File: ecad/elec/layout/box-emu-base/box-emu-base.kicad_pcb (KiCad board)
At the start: 2 copper layers, 72.5 x 63.9 mm, 66 parts

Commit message: feat(ecad): Update ecad / atopile and improve workflow
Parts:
- removed DS1: , lib:SOD-323_L1.8-W1.3-LS2.5-RD
- removed J1: , lib:CONN-SMD_4P-P1.00_SM04B-SRSS-TB-LF-SN
- removed R27: 62.5mW Thick Film Resistors 50V ±100ppm/℃ ±1% 249Ω 0402 Chi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, lib:R0402
- removed U10: , Connector_PinHeader_1.00mm:PinHeader_1x02_P1.00mm_Vertical
- removed U11: , lib:GAMEBOY_COLOR_DPAD_MEMBRANE
- removed U12, U13, U14, U15: , lib:GBC_DPAD_BUTTON
- removed U16, U19: , lib:GAMEBOY_COLOR_A_B_BUTTON_MEMBRANE
- removed U17, U18, U20, U21: , lib:GBC_A_B_BUTTON
- removed U22: , lib:GAMEBOY_COLOR_START_SELECT_MEMBRANE
- removed U23, U24: , lib:GBC_START_SELECT_BUTTON
- removed U25, U26: , lib:SW-SMD_TS24CA
- removed U7: , lib:DFN-8_L2.0-W2.0-P0.50-BL-EP
- removed U8: , lib:SIM-SMD_C9900007362
- removed U9: , lib:VSSOP-10_L3.0-W3.0-P0.50-LS4.9-BL
- added C10: 22µF ±20%, Samsung_Electro_Mechanics_CL21A226MAQNNNE:C0805, F.Cu at (300.0, -290.0)
- added C11: 22µF ±20%, Samsung_Electro_Mechanics_CL21A226MAQNNNE:C0805, F.Cu at (300.0, -300.0)
- added C12: 100nF ±10%, Samsung_Electro_Mechanics_CL05B104KO5NNNC:C0402, F.Cu at (300.0, -330.0)
- added C13: 100nF ±10%, Samsung_Electro_Mechanics_CL05B104KO5NNNC:C0402, F.Cu at (300.0, -340.0)
- added CN1: , JST_Sales_America_S2B_PH_SM4_TB_LF__SN:CONN-SMD_P2.00_S2B-PH-SM4-TB-LF-SN, B.Cu at (-11.2, 58.3)
- added CN2: , JST_Sales_America_SM04B_SRSS_TB_LF__SN:CONN-SMD_4P-P1.00_SM04B-SRSS-TB-LF-SN, F.Cu at (30.0, 0.00)
- added D1: , Guangdong_Hottech_1N5819WS:SOD-323_L1.8-W1.3-LS2.5-RD, F.Cu at (-14.1, 51.3)
- added H1: , Ckmtw_B_2100S02P_A110:HDR-TH_2P-P2.54-V-M-1, F.Cu at (1.15, 2.39)
- added MECH1: , GBC_A_B_MEMBRANE:GAMEBOY_COLOR_A_B_BUTTON_MEMBRANE, F.Cu at (21.2, 29.4)
- added MECH2: , GBC_A_B_MEMBRANE:GAMEBOY_COLOR_A_B_BUTTON_MEMBRANE, F.Cu at (15.9, 14.2)
- added MECH3: , GBC_DPAD_MEMBRANE:GAMEBOY_COLOR_DPAD_MEMBRANE, F.Cu at (-22.9, 21.8)
- added MECH4: , BOX_EMU_BASE_OUTLINE:BOX_EMU_BASE, F.Cu at (0.00, 0.00)
- added MECH5: , GBC_START_SELECT_MEMBRANE:GAMEBOY_COLOR_START_SELECT_MEMBRANE, F.Cu at (-1.52, 44.0)
- added SW1: , GBC_A_B_BUTTON:GBC_A_B_BUTTON, F.Cu at (28.1, 27.0)
- added SW10: , GBC_START_SELECT_BUTTON:GBC_START_SELECT_BUTTON, F.Cu at (4.70, 44.0)
- added SW11: , SHOU_HAN_TS24CA:SW-SMD_2P-TS24CA, F.Cu at (-21.8, 62.7)
- added SW12: , SHOU_HAN_TS24CA:SW-SMD_2P-TS24CA, F.Cu at (-15.8, 63.7)
- added SW2: , GBC_A_B_BUTTON:GBC_A_B_BUTTON, F.Cu at (14.2, 32.0)
- added SW3: , GBC_A_B_BUTTON:GBC_A_B_BUTTON, F.Cu at (23.0, 11.7)
- added SW4: , GBC_A_B_BUTTON:GBC_A_B_BUTTON, F.Cu at (9.01, 16.6)
- added SW5: , GBC_DPAD_BUTTON:GBC_DPAD_BUTTON, F.Cu at (-22.9, 29.8)
- added SW6: , GBC_DPAD_BUTTON:GBC_DPAD_BUTTON, F.Cu at (-30.9, 21.9)
- added SW7: , GBC_DPAD_BUTTON:GBC_DPAD_BUTTON, F.Cu at (-14.9, 21.9)
- added SW8: , GBC_DPAD_BUTTON:GBC_DPAD_BUTTON, F.Cu at (-22.9, 13.9)
- added SW9: , GBC_START_SELECT_BUTTON:GBC_START_SELECT_BUTTON, F.Cu at (-6.86, 44.0)
- added USB1: , Yuandi_TYPE_611_T3_W:USB-C-SMD_TYPE-611-T3-W, F.Cu at (-1.14, 63.9)
- C1: value 16V 100nF X7R ±10% 0402 Multilayer Ceramic Capacitors MLCC - SMD/SMT ROHS -> 100nF ±10%; footprint lib:C0402 -> Samsung_Electro_Mechanics_CL05B104KO5NNNC:C0402
- C2: value 25V 10uF X5R ±10% 0805 Multilayer Ceramic Capacitors MLCC - SMD/SMT ROHS -> 1µF ±10%; footprint lib:C0805 -> Samsung_Electro_Mechanics_CL05A105KA5NQNC:C0402
- C3, C4, C5: value 25V 10uF X5R ±10% 0805 Multilayer Ceramic Capacitors MLCC - SMD/SMT ROHS -> 100nF ±10%; footprint lib:C0805 -> Samsung_Electro_Mechanics_CL05B104KO5NNNC:C0402
- C6: value 16V 100nF X7R ±10% 0402 Multilayer Ceramic Capacitors MLCC - SMD/SMT ROHS -> 4.7µF ±10%; footprint lib:C0402 -> Samsung_Electro_Mechanics_CL05A475KP5NRNC:C0402
- C7: value 10V 4.7uF X5R ±20% 0402 Multilayer Ceramic Capacitors MLCC - SMD/SMT ROHS -> 4.7µF ±10%; footprint lib:C0402 -> Samsung_Electro_Mechanics_CL05A475KP5NRNC:C0402
- C8: value 10V 4.7uF X5R ±20% 0402 Multilayer Ceramic Capacitors MLCC - SMD/SMT ROHS -> 10µF ±10%; footprint lib:C0402 -> Samsung_Electro_Mechanics_CL21A106KAYNNNE:C0805
- C9: value 16V 100nF X7R ±10% 0402 Multilayer Ceramic Capacitors MLCC - SMD/SMT ROHS -> 10µF ±10%; footprint lib:C0402 -> Samsung_Electro_Mechanics_CL21A106KAYNNNE:C0805
- L1: footprint lib:IND-SMD_L2.5-W2.0_WPN252012H -> Sunlord_WPN252012H1R5MT:IND-SMD_L2.5-W2.0_WPN252012H
- LED1: footprint lib:LED0805-R-RD -> Yongyu_Photoelectric_SZYY0805R:LED0805-R-RD
- R1, R2: value 62.5mW Thick Film Resistors 50V ±100ppm/℃ ±1% 4.7kΩ 0402 Chip Resistor - Surface Mount ROHS -> 1MΩ ±1%; footprint lib:R0402 -> UNI_ROYAL_0402WGF1004TCE:R0402
- R10: value 62.5mW Thick Film Resistors 50V ±100ppm/℃ ±1% 2kΩ 0402 Chip Resistor - Surface Mount ROHS -> 10kΩ ±1%; footprint lib:R0402 -> UNI_ROYAL_0402WGF1002TCE:R0402
- R11: value 62.5mW Thick Film Resistors 50V ±100ppm/℃ ±1% 2.55kΩ 0402 Chip Resistor - Surface Mount ROHS -> 10kΩ ±1%; footprint lib:R0402 -> UNI_ROYAL_0402WGF1002TCE:R0402
- R12, R13, R14, R15, R16, R18, R19, R20, R25, R3, R4, R5, R6: value 62.5mW Thick Film Resistors 50V ±100ppm/℃ ±1% 10kΩ 0402 Chip Resistor - Surface Mount ROHS -> 10kΩ ±1%; footprint lib:R0402 -> UNI_ROYAL_0402WGF1002TCE:R0402
- R17, R23, R24: value 62.5mW Thick Film Resistors 50V ±100ppm/℃ ±1% 10kΩ 0402 Chip Resistor - Surface Mount ROHS -> 5.1kΩ ±1%; footprint lib:R0402 -> UNI_ROYAL_0402WGF5101TCE:R0402
- R21: value 62.5mW Thick Film Resistors 50V ±100ppm/℃ ±1% 10kΩ 0402 Chip Resistor - Surface Mount ROHS -> 91kΩ ±1%; footprint lib:R0402 -> YAGEO_RC0402FR_0791KL:R0402
- R22: value 62.5mW Thick Film Resistors 50V ±100ppm/℃ ±1% 10kΩ 0402 Chip Resistor - Surface Mount ROHS -> 820kΩ ±1%; footprint lib:R0402 -> FOJAN_FRC0402F8203TS:R0402
- R26: value 62.5mW Thick Film Resistors 50V ±100ppm/℃ ±1% 255Ω 0402 Chip Resistor - Surface Mount ROHS -> 10kΩ ±1%; footprint lib:R0402 -> UNI_ROYAL_0402WGF1002TCE:R0402
- R7: value 62.5mW Thick Film Resistors ±100ppm/℃ ±1% 243kΩ 0402 Chip Resistor - Surface Mount ROHS -> 2kΩ ±1%; footprint lib:R0402 -> UNI_ROYAL_0402WGF2001TCE:R0402
- R8: value 62.5mW Thick Film Resistors 50V ±100ppm/℃ ±1% 27.4kΩ 0402 Chip Resistor - Surface Mount ROHS -> 10kΩ ±1%; footprint lib:R0402 -> UNI_ROYAL_0402WGF1002TCE:R0402
- R9: value 62.5mW Thick Film Resistors 50V ±100ppm/℃ ±1% 1MΩ 0402 Chip Resistor - Surface Mount ROHS -> 10kΩ ±1%; footprint lib:R0402 -> UNI_ROYAL_0402WGF1002TCE:R0402
- U1: footprint lib:BOX_EMU_BASE -> Texas_Instruments_DRV2605LDGSR:VSSOP-10_L3.0-W3.0-P0.50-LS4.9-BL
- U2: footprint lib:CONN-SMD_P2.00_S2B-PH-SM4-TB-LF-SN -> AWINIC_AW9523BTQR:VFQFPN-24_L4.0-W4.0-P0.50-BL-EP2.8; moved to F.Cu
- U3: footprint lib:USB-C-SMD_TYPE-611-T3-W -> Maxim_Integrated_MAX17048G_T10:TDFN-8_L2.0-W2.0-P0.50-BL-EP1.2
- U4: footprint lib:VFQFPN-24_L4.0-W4.0-P0.50-BL-EP2.8 -> Microchip_Tech_MCP73831T_2ACI_OT:SOT-23-5_L3.0-W1.7-P0.95-LS2.8-BL
- U5: footprint lib:VSON-14_L4.0-W3.0-P0.50-BL-EP_TI_DSJ -> Texas_Instruments_TPS63020DSJR:VSON-14_L4.0-W3.0-P0.50-BL-EP_TI_DSJ
- U6: footprint lib:SOT-23-5_L3.0-W1.7-P0.95-LS2.8-BL -> HOAUC_HYCW118_TF09_200B:SIM-SMD_C9900007362
- moved R25 509.1 mm to (300.0, -370.0), turned to 0 degrees
- moved R26 506.9 mm to (300.0, -380.0), turned to 0 degrees
- moved R24 499.4 mm to (300.0, -360.0), turned to 0 degrees
- moved R23 469.6 mm to (300.0, -350.0), turned to 0 degrees
- moved R22 438.0 mm to (300.0, -320.0)
- moved C9 421.2 mm to (300.0, -280.0), turned to 0 degrees
- moved C8 411.4 mm to (300.0, -270.0), turned to 0 degrees
- moved R21 396.1 mm to (300.0, -310.0), turned to 0 degrees
- moved C6 383.1 mm to (300.0, -240.0), turned to 0 degrees
- moved C7 375.2 mm to (300.0, -230.0), turned to 0 degrees
- moved C5 370.9 mm to (300.0, -220.0), turned to 0 degrees
- moved R18 329.9 mm to (300.0, -210.0), turned to 0 degrees
- moved C4 328.9 mm to (300.0, -170.0), turned to 0 degrees
- moved R17 318.9 mm to (300.0, -200.0), turned to 0 degrees
- moved R16 314.2 mm to (300.0, -190.0), turned to 0 degrees
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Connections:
- net l1 renamed 1
- net l2 renamed 2
- C1 pad 1: vcc_3v3 -> battery_measurement
- C2 pad 1: vbat -> hv
- C3 pad 1: vbat -> vcc_3v3
- C4 pad 1: vcc_5v -> vcc_3v3
- C5 pad 1: vcc_5v -> vbat
- C6 pad 1: vina -> vbat
- LED1 pad 1: vbus -> pos
- LED1 pad 2: cathode -> STAT
- R1 pad 1: cc1 -> battery_measurement
- R10 pad 1: prog -> vcc_3v3
- R10 pad 2: gnd -> right
- R11 pad 1: cathode -> vcc_3v3
- R11 pad 2: mcp73831-gnd -> up
- R12 pad 1: p1_3 -> EN
- R13 pad 1: en -> vcc_3v3
- R13 pad 2: vcc_3v3 -> SCL
- R14 pad 2: up -> SDA
- R15 pad 2: down -> INTN
- R16 pad 2: left -> RSTN
- R17 pad 1: vcc_3v3 -> vbus
- R17 pad 2: right -> pos
- R18 pad 1: vcc_3v3 -> nALRT
- R18 pad 2: io-a -> vcc_3v3
- R19 pad 2: io-b -> select
- R2 pad 1: cc2 -> vbat
- R2 pad 2: gnd -> battery_measurement
- R20 pad 2: x -> start
- R21 pad 1: vcc_3v3 -> FB
- R21 pad 2: y -> gnd
- R22 pad 1: vcc_3v3 -> vcc_5v
- R22 pad 2: start -> FB
- R23 pad 1: vcc_3v3 -> A5
- R23 pad 2: select -> gnd
- R24 pad 1: vcc_3v3 -> B5
- R24 pad 2: vol_up -> gnd
- R26 pad 1: vbat -> vcc_3v3
- R26 pad 2: battery_measurement -> vol_up
- R3 pad 1: sda -> vcc_3v3
- R3 pad 2: vcc_3v3 -> line
- R4 pad 1: scl -> vcc_3v3
- R4 pad 2: vcc_3v3 -> buttons_abxy-b-line
- R5 pad 2: rstn -> x_y_btns-a-line
- R6 pad 2: intn -> x_y_btns-b-line
- R7 pad 1: vcc_5v -> PROG
- R7 pad 2: out -> gnd
- R8 pad 1: out -> vcc_3v3
- R8 pad 2: gnd -> down
- R9 pad 1: pg -> vcc_3v3
- R9 pad 2: gnd -> left
- U2 pad 1: vbat -> start
- U2 pad 2: gnd -> select
- U2 pad 3: gnd -> 3
- U2 pad 4: gnd -> nALRT
- U4 pad 1: start -> STAT
- U4 pad 2: select -> gnd
- U4 pad 3: p1_2 -> vbat
- U4 pad 4: p1_3 -> vbus
- U4 pad 5: up -> PROG
- U5 pad 1: vina -> vbat
- U5 pad 12: vina -> vbat
- U5 pad 14: pg -> PG
- U5 pad 3: out -> FB
- U6 pad 1: mcp73831-gnd -> uSD.card-1
- U6 pad 2: gnd -> cs-2
- U6 pad 3: vbat -> MOSI
- U6 pad 4: vbus -> vcc_3v3
- U6 pad 5: prog -> SCLK
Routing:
- net gnd: track 441.3 -> 0.00 mm, vias 13 -> 0
- net vcc_3v3: track 161.0 -> 0.00 mm, vias 16 -> 0
- net sda: track 136.9 -> 0.00 mm, vias 6 -> 0
- net scl: track 130.2 -> 0.00 mm, vias 4 -> 0
- net io-b: track 77.7 -> 0.00 mm
- net down: track 69.4 -> 0.00 mm, vias 2 -> 0
- net vbus: track 68.5 -> 0.00 mm, vias 4 -> 0
- net dm: track 67.2 -> 0.00 mm, vias 1 -> 0
- net miso: track 66.3 -> 0.00 mm, vias 1 -> 0
- net dp: track 65.5 -> 0.00 mm, vias 1 -> 0
- net y: track 63.1 -> 0.00 mm
- net sck: track 62.0 -> 0.00 mm, vias 1 -> 0
- net mosi: track 57.5 -> 0.00 mm, vias 1 -> 0
- net battery_measurement: track 56.2 -> 0.00 mm, vias 1 -> 0
- net cs: track 55.1 -> 0.00 mm, vias 1 -> 0
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- removed copper zone on F.Cu, net gnd
- removed copper zone on B.Cu, net vcc_3v3
- removed copper zone on B.Cu, net vcc_5v
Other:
- board text removed: "A"
- board text removed: "B"
- board text removed: "DOWN"
- board text removed: "LEFT"
- board text removed: "RIGHT"
- board text removed: "SELECT"
- board text removed: "START"
- board text removed: "UP"
- board text removed: "X"
- board text removed: "Y"

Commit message: improve workflow
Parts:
- moved U6 11.4 mm to (13.2, 58.2), turned to 6 degrees
- moved USB1 1.54 mm to (-1.14, 62.3)
- moved CN1 0.46 mm to (-11.0, 58.7), turned to 0 degrees
- turned SW11 to 170 degrees
- turned SW12 to 174 degrees
- turned SW3 to 180 degrees
- turned SW4 to 180 degrees
- turned SW5 to 90 degrees
- turned SW7 to 180 degrees
- turned SW8 to 270 degrees

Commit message: improve placement of components and robustness of scripts
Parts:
- MECH1, MECH2: value (none) -> SILKSCREENGBC_A/B
- REF**: renamed from MECH4; value (none) -> BOX_EMU_BASE
- U$1: renamed from MECH3; value (none) -> SILKSCREENGBC_D-PAD
- U$2: renamed from MECH5; value (none) -> SILKSCREENGBC_START/SELECT
- moved R24 515.7 mm to (133.3, 128.1), turned to 180 degrees
- moved R26 512.1 mm to (131.8, 103.6), turned to 180 degrees
- moved R23 507.4 mm to (133.3, 129.3), turned to 180 degrees
- moved R25 501.5 mm to (131.8, 102.4), turned to 180 degrees
- moved C13 487.4 mm to (147.1, 122.8), turned to 180 degrees
- moved C12 485.7 mm to (129.9, 124.9)
- moved R22 479.8 mm to (115.6, 123.0), turned to 180 degrees
- moved R21 469.5 mm to (115.6, 121.8), turned to 180 degrees
- moved C11 455.4 mm to (120.4, 118.5), turned to 90 degrees
- moved C9 442.5 mm to (121.2, 124.8), turned to 180 degrees
- moved C8 432.2 mm to (111.1, 118.7), turned to 90 degrees
- moved C6 408.1 mm to (105.2, 118.6), turned to 90 degrees
- moved C10 407.8 mm to (122.3, 77.0), turned to 90 degrees
- moved C7 398.1 mm to (127.5, 128.8)
- moved C5 392.7 mm to (124.7, 131.4)
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- renumbered SW1 to U2, SW2 to U2, SW3 to U2, SW4 to U2, SW10 to U3, SW9 to U3, SW8 to U5, SW5 to U5, SW7 to U5, SW6 to U5
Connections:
- net buttons_abxy-b-line renamed b-line

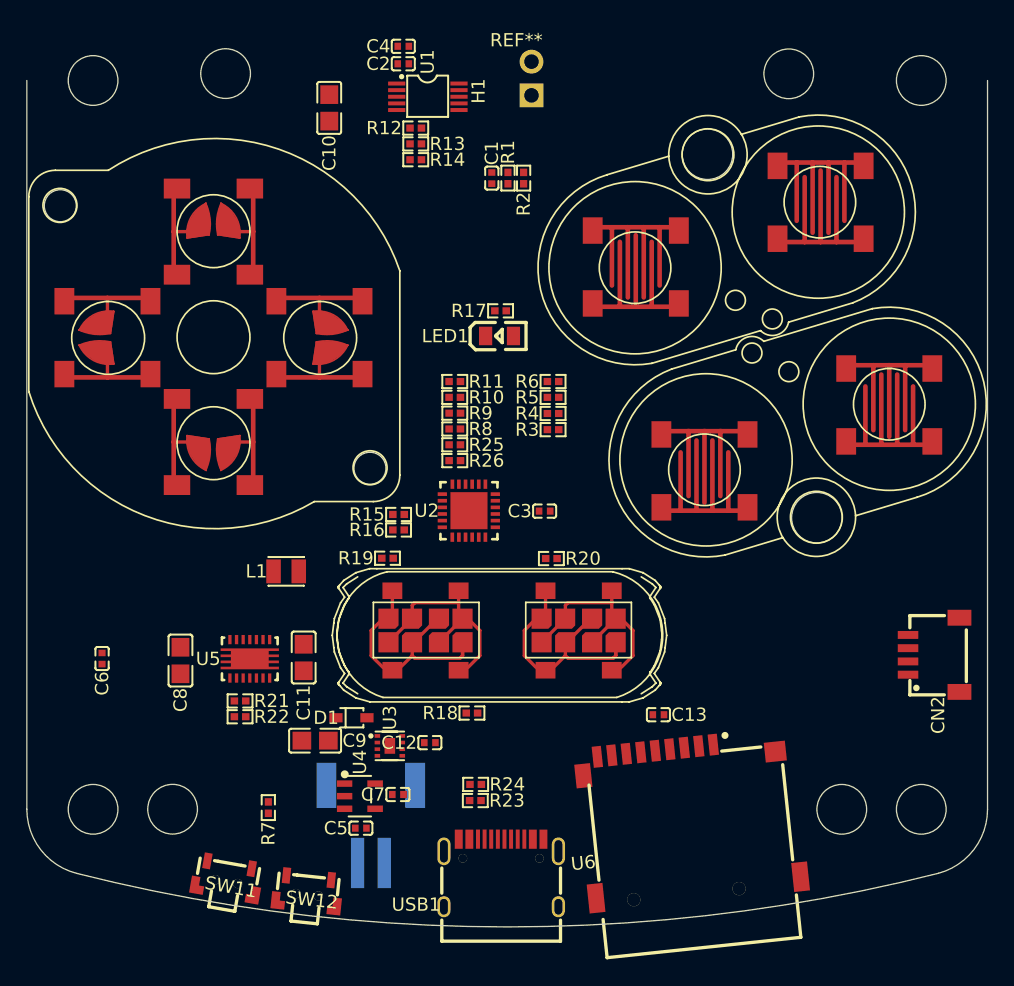
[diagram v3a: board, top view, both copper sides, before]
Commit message: nudge layouts some
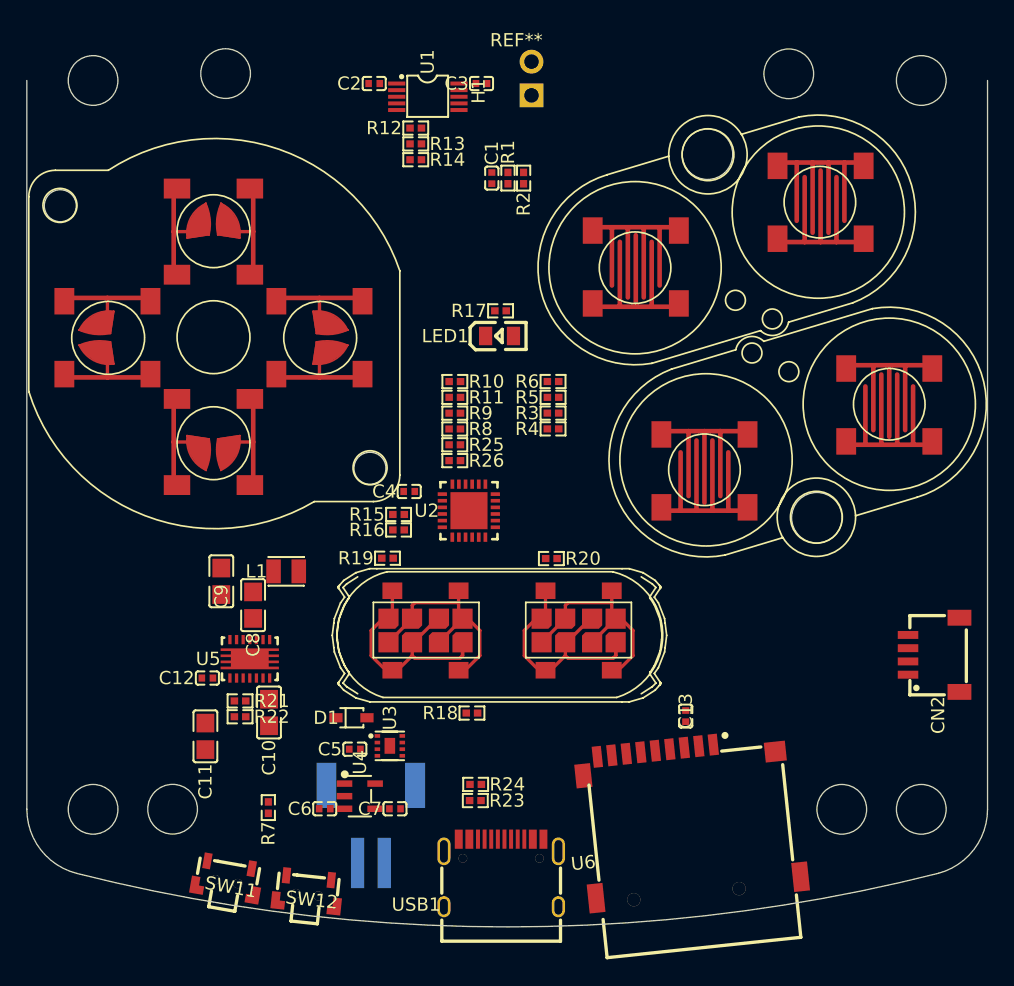
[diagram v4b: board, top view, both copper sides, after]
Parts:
- MECH1, MECH2: value SILKSCREENGBC_A/B -> (none)
- REF**: value BOX_EMU_BASE -> (none)
- U$1: value SILKSCREENGBC_D-PAD -> (none)
- U$2: value SILKSCREENGBC_START/SELECT -> (none)
- moved C10 45.9 mm to (117.8, 122.6)
- moved C4 33.6 mm to (128.3, 106.0)
- moved C3 32.6 mm to (133.8, 75.2)
- moved C6 20.3 mm to (122.0, 129.9), turned to 0 degrees
- moved C12 17.5 mm to (113.1, 120.0)
- moved C9 14.0 mm to (114.2, 112.7), turned to 90 degrees
- moved C11 9.51 mm to (113.0, 124.4)
- moved C8 6.89 mm to (116.6, 114.5)
- moved C5 5.98 mm to (124.2, 125.4)
- moved C2 2.65 mm to (125.7, 75.2)
- moved C13 2.06 mm to (149.2, 122.9), turned to 90 degrees
- moved R3 1.25 mm to (139.2, 100.0)
- moved R11 1.19 mm to (131.8, 98.9)
- moved R10 1.19 mm to (131.8, 97.7)
- moved R4 1.16 mm to (139.2, 101.2)
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- renumbered U2 to SW1, U3 to SW10, U2 to SW2, U2 to SW3, U2 to SW4, U5 to SW5, U5 to SW6, U5 to SW7, U5 to SW8, U3 to SW9

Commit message: further layout changes
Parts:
- moved L1 6.66 mm to (120.0, 118.6), turned to 270 degrees
- moved C11 3.45 mm to (116.4, 124.5), turned to 180 degrees
- moved R22 2.15 mm to (113.7, 121.9)
- moved R21 2.14 mm to (113.7, 122.8), turned to 0 degrees
- moved C9 2.04 mm to (116.0, 113.6), turned to 180 degrees
- moved C10 1.36 mm to (116.4, 122.7), turned to 180 degrees
- moved C8 1.02 mm to (116.0, 115.4), turned to 180 degrees
- turned C12 to 180 degrees
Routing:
- net gnd: track 0.00 -> 21.5 mm
- net vcc_5v: track 0.00 -> 11.1 mm
- net vbat: track 0.00 -> 7.45 mm
- net FB: track 0.00 -> 5.30 mm
- net 2: track 0.00 -> 3.14 mm
- net 1: track 0.00 -> 3.14 mm

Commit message: fixing some issues
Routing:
- net gnd: track 21.5 -> 3.71 mm
- net vcc_5v: track 11.1 -> 4.04 mm
- net 2: track 3.14 -> 0.00 mm
- net 1: track 3.14 -> 0.00 mm
- net vbat: track 7.45 -> 5.69 mm, vias 0 -> 2
- added copper zone on F.Cu, net 1
- added copper zone on F.Cu, net 2
- added copper zone on F.Cu, net gnd
- added copper zone on F.Cu, net vbat
- added copper zone on F.Cu, net vcc_5v
